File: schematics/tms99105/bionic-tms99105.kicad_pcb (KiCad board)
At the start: 2 copper layers, 25.4 x 68.6 mm, 8 parts, among them J1 Bionic-P135, J2 Bionic-P245, U1 TMS99105, U2 11AA010-I/TT

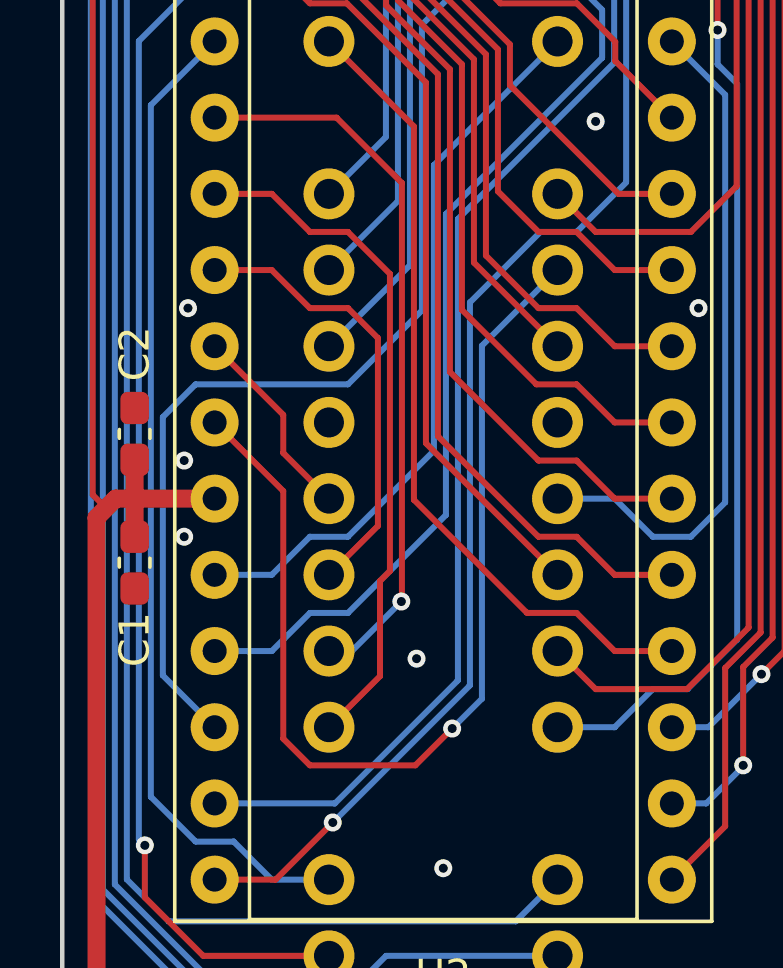
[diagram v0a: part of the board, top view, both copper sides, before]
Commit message: [tms9900] Add automation config
The TMS9980, TMS9995, TMS99105 and TMS99110 run TMS9900 code. Fix the
TMS9980's program memory writes and the TMS9995's on-chip memory map.
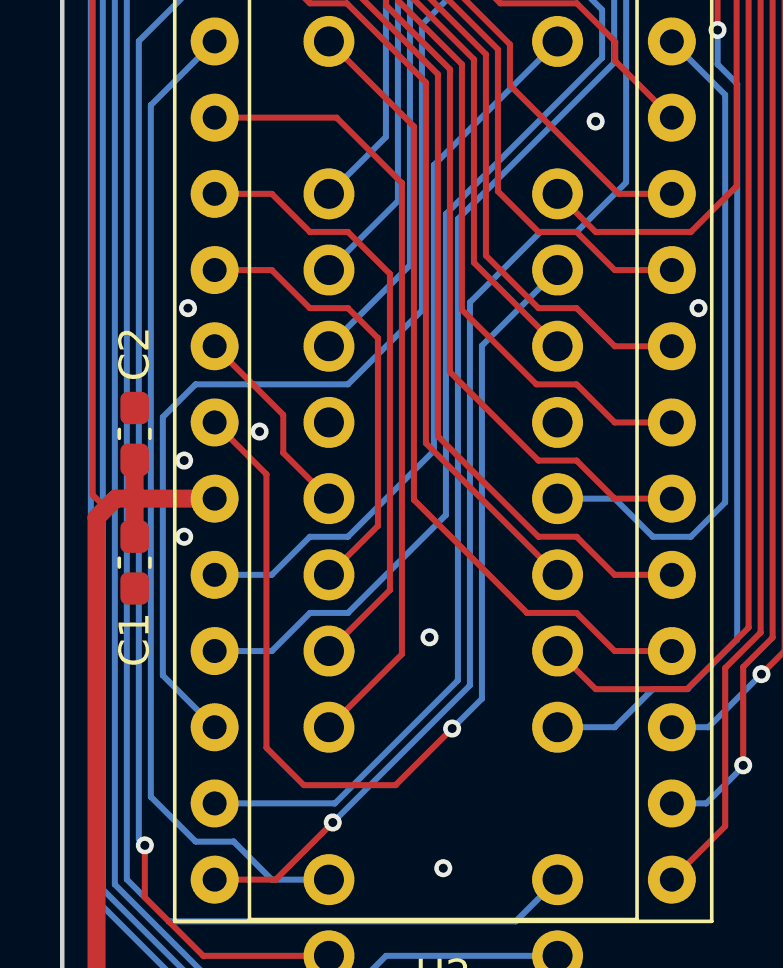
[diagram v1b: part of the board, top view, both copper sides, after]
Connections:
- J1 pad 14: (no net) -> unconnected-(J1-P33-Pad14)
- J1 pad 17: /P37 -> /P36
- J1 pad 18: /P36 -> /P37
- J2 pad 26: unconnected-(U2-SCIO-Pad1) -> Net-(J2-P57)
- J2 pad 27: (no net) -> unconnected-(J2-P56-Pad27)
- J2 pad 35: (no net) -> unconnected-(J2-P43-Pad35)
- U2 pad 1: unconnected-(U2-SCIO-Pad1) -> Net-(J2-P57)
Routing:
- net unconnected-(U2-SCIO-Pad1): track 4.32 -> 0.00 mm
- net Net-(J2-P57): track 0.00 -> 4.32 mm
- net /P37: track 24.2 -> 26.3 mm, vias 1 -> 0
- net /P36: track 22.9 -> 21.1 mm
- net /P41: track 34.7 -> 35.8 mm
- net GND: vias 12 -> 13
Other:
- board text added: "Rev. 4"
- board text removed: "Rev. 3"
